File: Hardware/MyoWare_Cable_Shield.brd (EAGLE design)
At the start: 52.3 x 20.8 mm, 13 parts

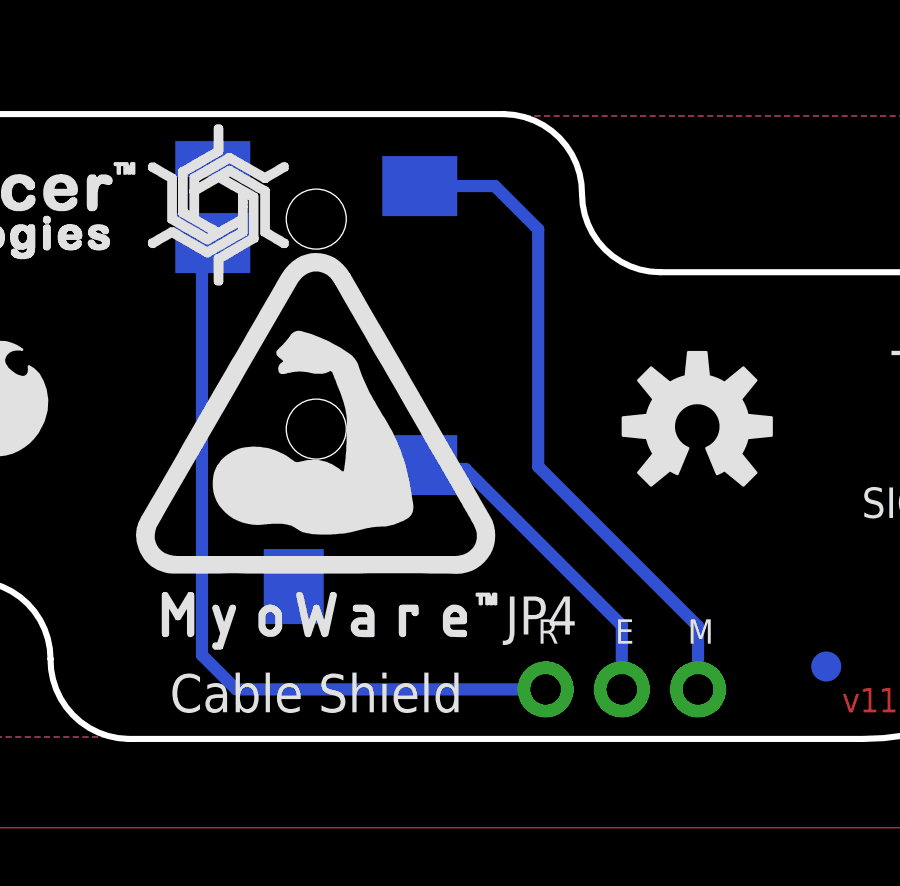
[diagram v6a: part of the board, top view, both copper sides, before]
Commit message: Rewiring of 3.5mm Jack
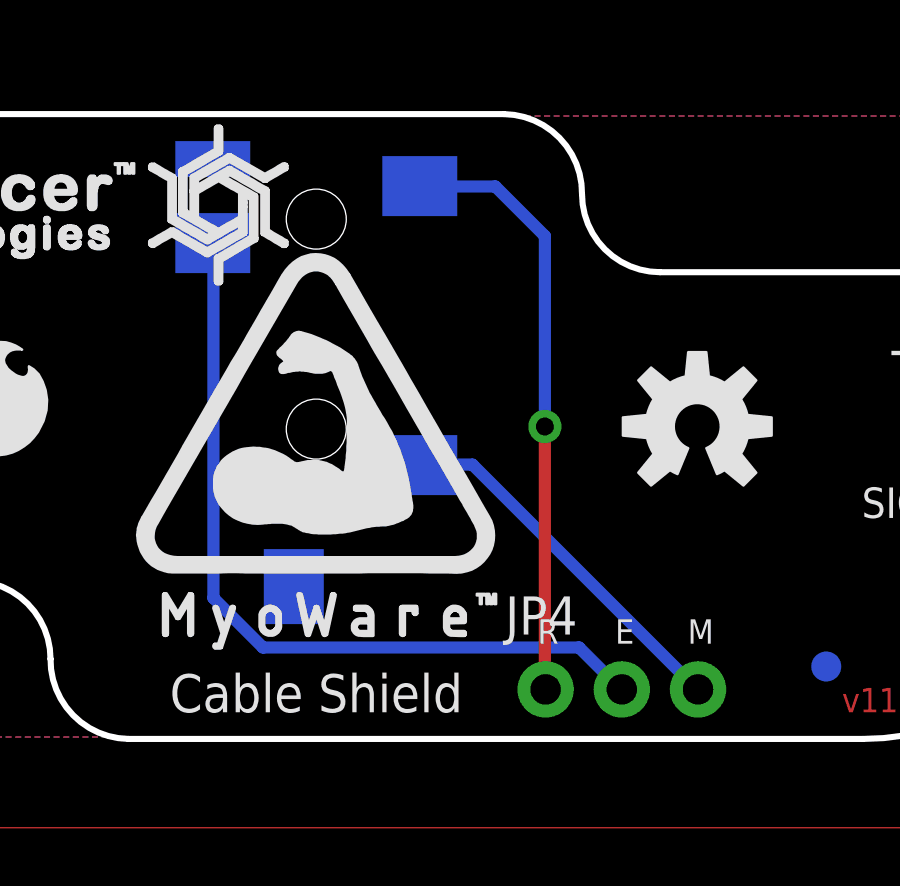
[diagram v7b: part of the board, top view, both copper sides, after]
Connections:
- net END: now also JP3.RING; no longer JP3.TIP
- net MID: now also JP3.TIP; no longer JP3.SLEEVE
- net VREF: now also JP3.SLEEVE; no longer JP3.RING
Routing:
- net END: track 11.2 -> 26.7 mm, vias 0 -> 1
- net MID: track 22.1 -> 12.4 mm
- net VREF: track 25.9 -> 20.0 mm, vias 0 -> 1
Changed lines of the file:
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@@
 <setting verticaltext="up"/>
 </settings>
-<grid distance="0.05" unitdist="inch" unit="inch" style="lines" multiple="1" display="yes" altdistance="0.005" altunitdist="inch" altunit="inch"/>
+<grid distance="0.005" unitdist="inch" unit="inch" style="lines" multiple="1" display="yes" altdistance="0.005" altunitdist="inch" altunit="inch"/>
 <layers>
 <layer number="1" name="Top" color="4" fill="1" visible="yes" active="yes"/>
@@
 <wire x1="1.5875" y1="12.954" x2="4.1275" y2="12.954" width="0.4064" layer="1"/>
 </signal>
-<signal name="MID">
-<contactref element="JP4" pad="3"/>
-<wire x1="33.55975" y1="16.98625" x2="33.55975" y2="9.077959375" width="0.4064" layer="16"/>
-<wire x1="33.55975" y1="9.077959375" x2="38.8874" y2="3.750309375" width="0.4064" layer="16"/>
-<contactref element="JP3" pad="SLEEVE"/>
-<wire x1="29.612" y1="18.428" x2="32.118" y2="18.428" width="0.4064" layer="16"/>
-<wire x1="32.118" y1="18.428" x2="33.55975" y2="16.98625" width="0.4064" layer="16"/>
-<wire x1="38.8874" y1="1.651" x2="38.8874" y2="3.750309375" width="0.4064" layer="16"/>
-</signal>
-<signal name="END">
-<contactref element="JP4" pad="2"/>
-<wire x1="36.3474" y1="3.7846" x2="31.133034375" y2="8.999" width="0.4064" layer="16"/>
-<contactref element="JP3" pad="TIP"/>
-<wire x1="31.133034375" y1="8.999" x2="29.61513125" y2="8.999" width="0.4064" layer="16"/>
-<wire x1="29.61513125" y1="8.999" x2="29.612" y2="9.128" width="0.4064" layer="16"/>
-<wire x1="36.3474" y1="1.651" x2="36.3474" y2="3.7846" width="0.4064" layer="16"/>
-</signal>
-<signal name="VREF">
-<contactref element="JP4" pad="1"/>
-<wire x1="33.8074" y1="1.651" x2="23.495" y2="1.651" width="0.4064" layer="16"/>
-<wire x1="23.495" y1="1.651" x2="22.352" y2="2.794" width="0.4064" layer="16"/>
-<wire x1="22.352" y1="2.794" x2="22.352" y2="16.389" width="0.4064" layer="16"/>
-<contactref element="JP3" pad="RING"/>
-<wire x1="22.352" y1="16.389" x2="22.491" y2="16.528" width="0.4064" layer="16"/>
-<wire x1="22.491" y1="16.528" x2="22.712" y2="16.528" width="0.4064" layer="16"/>
-</signal>
 <signal name="SIG">
 <contactref element="JP6" pad="3"/>
@@
 <wire x1="0" y1="83.9" x2="0" y2="-2.96" width="0" layer="1"/>
 </signal>
+<signal name="MID">
+<contactref element="JP4" pad="3"/>
+<contactref element="JP3" pad="TIP"/>
+<wire x1="38.8874" y1="1.651" x2="38.862" y2="1.651" width="0.4064" layer="16"/>
+<wire x1="38.862" y1="1.651" x2="31.369" y2="9.144" width="0.4064" layer="16"/>
+<wire x1="31.369" y1="9.144" x2="29.628" y2="9.144" width="0.4064" layer="16"/>
+<wire x1="29.628" y1="9.144" x2="29.612" y2="9.128" width="0.4064" layer="16"/>
+</signal>
+<signal name="VREF">
+<contactref element="JP3" pad="SLEEVE"/>
+<contactref element="JP4" pad="1"/>
+<wire x1="29.612" y1="18.428" x2="29.612" y2="18.415" width="0.4064" layer="16"/>
+<wire x1="29.612" y1="18.415" x2="32.131" y2="18.415" width="0.4064" layer="16"/>
+<wire x1="32.131" y1="18.415" x2="33.782" y2="16.764" width="0.4064" layer="16"/>
+<wire x1="33.782" y1="16.764" x2="33.782" y2="10.414" width="0.4064" layer="16"/>
+<via x="33.782" y="10.414" extent="1-16" drill="0.6" shape="square"/>
+<wire x1="33.782" y1="10.414" x2="33.782" y2="1.6764" width="0.4064" layer="1"/>
+<wire x1="33.782" y1="1.6764" x2="33.8074" y2="1.651" width="0.4064" layer="1"/>
+</signal>
+<signal name="END">
+<contactref element="JP4" pad="2"/>
+<contactref element="JP3" pad="RING"/>
+<wire x1="36.3474" y1="1.651" x2="36.322" y2="1.651" width="0.4064" layer="1"/>
+<wire x1="36.322" y1="1.651" x2="34.925" y2="3.048" width="0.4064" layer="16"/>
+<via x="36.322" y="1.651" extent="1-16" drill="0.6" shape="square"/>
+<wire x1="34.925" y1="3.048" x2="24.384" y2="3.048" width="0.4064" layer="16"/>
+<wire x1="24.384" y1="3.048" x2="22.733" y2="4.699" width="0.4064" layer="16"/>
+<wire x1="22.733" y1="4.699" x2="22.733" y2="16.507" width="0.4064" layer="16"/>
+<wire x1="22.733" y1="16.507" x2="22.712" y2="16.528" width="0.4064" layer="16"/>
+</signal>
 </signals>

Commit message: Design Review Changes
Via to top board change to round instead of square
Dimensions on board fixed
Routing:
- net N$3: track 664.4 -> 0.00 mm
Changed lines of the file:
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@@
 <layer number="17" name="Pads" color="2" fill="1" visible="yes" active="yes"/>
 <layer number="18" name="Vias" color="2" fill="1" visible="yes" active="yes"/>
-<layer number="19" name="Unrouted" color="6" fill="1" visible="yes" active="yes"/>
-<layer number="20" name="Dimension" color="15" fill="1" visible="yes" active="yes"/>
-<layer number="21" name="tPlace" color="16" fill="1" visible="yes" active="yes"/>
+<layer number="19" name="Unrouted" color="6" fill="1" visible="no" active="yes"/>
+<layer number="20" name="Dimension" color="15" fill="1" visible="no" active="yes"/>
+<layer number="21" name="tPlace" color="16" fill="1" visible="no" active="yes"/>
 <layer number="22" name="bPlace" color="14" fill="1" visible="yes" active="yes"/>
 <layer number="23" name="tOrigins" color="15" fill="1" visible="yes" active="yes"/>
 <layer number="24" name="bOrigins" color="15" fill="1" visible="yes" active="yes"/>
-<layer number="25" name="tNames" color="7" fill="1" visible="no" active="yes"/>
-<layer number="26" name="bNames" color="7" fill="1" visible="no" active="yes"/>
-<layer number="27" name="tValues" color="7" fill="1" visible="no" active="yes"/>
-<layer number="28" name="bValues" color="7" fill="1" visible="no" active="yes"/>
+<layer number="25" name="tNames" color="7" fill="1" visible="yes" active="yes"/>
+<layer number="26" name="bNames" color="7" fill="1" visible="yes" active="yes"/>
+<layer number="27" name="tValues" color="7" fill="1" visible="yes" active="yes"/>
+<layer number="28" name="bValues" color="7" fill="1" visible="yes" active="yes"/>
 <layer number="29" name="tStop" color="7" fill="3" visible="no" active="yes"/>
 <layer number="30" name="bStop" color="7" fill="6" visible="no" active="yes"/>
@@
 <layer number="42" name="bRestrict" color="1" fill="10" visible="no" active="yes"/>
 <layer number="43" name="vRestrict" color="2" fill="10" visible="no" active="yes"/>
-<layer number="44" name="Drills" color="7" fill="1" visible="no" active="yes"/>
+<layer number="44" name="Drills" color="7" fill="1" visible="yes" active="yes"/>
 <layer number="45" name="Holes" color="7" fill="1" visible="yes" active="yes"/>
 <layer number="46" name="Milling" color="3" fill="1" visible="no" active="yes"/>
-<layer number="47" name="Measures" color="7" fill="1" visible="no" active="yes"/>
+<layer number="47" name="Measures" color="7" fill="1" visible="yes" active="yes"/>
 <layer number="48" name="Document" color="7" fill="1" visible="no" active="yes"/>
 <layer number="49" name="Reference" color="3" fill="1" visible="no" active="yes"/>
 <layer number="51" name="tDocu" color="6" fill="1" visible="yes" active="yes"/>
-<layer number="52" name="bDocu" color="7" fill="1" visible="no" active="yes"/>
+<layer number="52" name="bDocu" color="7" fill="1" visible="yes" active="yes"/>
 <layer number="3" name="Route3" color="4" fill="3" visible="no" active="no"/>
 <layer number="4" name="Route4" color="1" fill="4" visible="no" active="no"/>
@@
 <text x="46.3042" y="7.874" size="1.016" layer="22" font="vector" ratio="17" rot="MR180" align="center-right">SIG</text>
 <text x="46.3042" y="10.414" size="1.27" layer="22" font="vector" ratio="17" rot="MR180" align="center-right">-</text>
-<dimension x1="22.44725" y1="-6.477" x2="-21.74875" y2="6.477" x3="-27.9908" y3="0" textsize="1.778" textratio="15" layer="47" dtype="vertical" unit="inch"/>
 <text x="0" y="20.828" size="1.778" layer="47" font="vector" ratio="15" align="center">All units in inches</text>
 <text x="6.2738" y="12.954" size="1.016" layer="22" font="vector" ratio="17" rot="MR0" align="center-right">RAW</text>
@@
 <text x="36.27755" y="3.175" size="0.8128" layer="22" font="vector" ratio="20" rot="MR0" align="bottom-center">E</text>
 <wire x1="50.673" y1="15.5575" x2="52.324" y2="14.0335" width="0.2032" layer="20" curve="-90"/>
-<dimension x1="-6.25475" y1="-10.414" x2="-18.2245" y2="10.414" x3="-34.29" y3="0" textsize="1.778" textratio="15" layer="47" dtype="vertical" unit="inch"/>
-<dimension x1="-26.162" y1="2.54" x2="26.162" y2="3.6195" x3="0" y3="16.256" textsize="1.778" textratio="15" layer="47" dtype="horizontal" unit="inch"/>
-<dimension x1="-22.1615" y1="6.477" x2="22.1615" y2="-6.477" x3="0" y3="12.446" textsize="1.778" textratio="15" layer="47" dtype="horizontal" unit="inch"/>
-<dimension x1="-26.162" y1="2.54" x2="-22.1615" y2="6.477" x3="-24.16175" y3="12.446" textsize="1.778" layer="47" dtype="horizontal"/>
-<dimension x1="-18.2245" y1="10.414" x2="-22.1615" y2="6.477" x3="-31.496" y3="8.4455" textsize="1.778" layer="47" dtype="vertical"/>
-<dimension x1="18.2245" y1="-10.414" x2="22.1615" y2="-6.477" x3="29.464" y3="-8.4455" textsize="1.778" layer="47" dtype="vertical"/>
-<dimension x1="26.162" y1="-2.54" x2="22.1615" y2="-6.477" x3="24.16175" y3="-13.716" textsize="1.778" layer="47" dtype="horizontal"/>
 <polygon width="0.076" layer="21">
 <vertex x="30.83" y="5.54"/>
@@
 <vertex x="19.825" y="18.841"/>
 </polygon>
+<dimension x1="1.5875" y1="12.954" x2="1.5875" y2="10.414" x3="-4.699" y3="11.684" textsize="1.778" layer="20"/>
+<dimension x1="0.127" y1="20.7645" x2="0.127" y2="0.0635" x3="-12.319" y3="10.414" textsize="1.778" layer="20"/>
+<dimension x1="0.127" y1="0.0635" x2="52.197" y2="0.635" x3="26.162" y3="-4.064" textsize="1.778" layer="20" dtype="horizontal"/>
+<dimension x1="4.0005" y1="16.891" x2="0" y2="12.954" x3="2.00025" y3="24.765" textsize="1.778" layer="20" dtype="horizontal"/>
+<dimension x1="48.3235" y1="3.937" x2="52.324" y2="4.191" x3="50.32375" y3="-5.588" textsize="1.778" layer="20" dtype="horizontal"/>
+<dimension x1="1.5875" y1="10.414" x2="1.5875" y2="7.874" x3="-8.001" y3="9.144" textsize="1.778" layer="20" dtype="horizontal"/>
 </plain>
 <attributes>
@@
 <wire x1="48.1965" y1="12.954" x2="50.7365" y2="12.954" width="0.4064" layer="1"/>
 </signal>
-<signal name="N$3">
-<wire x1="0" y1="-2.96" x2="245.33" y2="-2.96" width="0" layer="1"/>
-<wire x1="245.33" y1="-2.96" x2="245.33" y2="83.9" width="0" layer="1"/>
-<wire x1="245.33" y1="83.9" x2="0" y2="83.9" width="0" layer="1"/>
-<wire x1="0" y1="83.9" x2="0" y2="-2.96" width="0" layer="1"/>
-</signal>
 <signal name="MID">
 <contactref element="JP4" pad="3"/>
@@
 <wire x1="32.131" y1="18.415" x2="33.782" y2="16.764" width="0.4064" layer="16"/>
 <wire x1="33.782" y1="16.764" x2="33.782" y2="10.414" width="0.4064" layer="16"/>
-<via x="33.782" y="10.414" extent="1-16" drill="0.6" shape="square"/>
+<via x="33.782" y="10.414" extent="1-16" drill="0.6"/>
 <wire x1="33.782" y1="10.414" x2="33.782" y2="1.6764" width="0.4064" layer="1"/>
 <wire x1="33.782" y1="1.6764" x2="33.8074" y2="1.651" width="0.4064" layer="1"/>
